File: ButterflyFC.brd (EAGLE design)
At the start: 100 x 80 mm, 7 parts

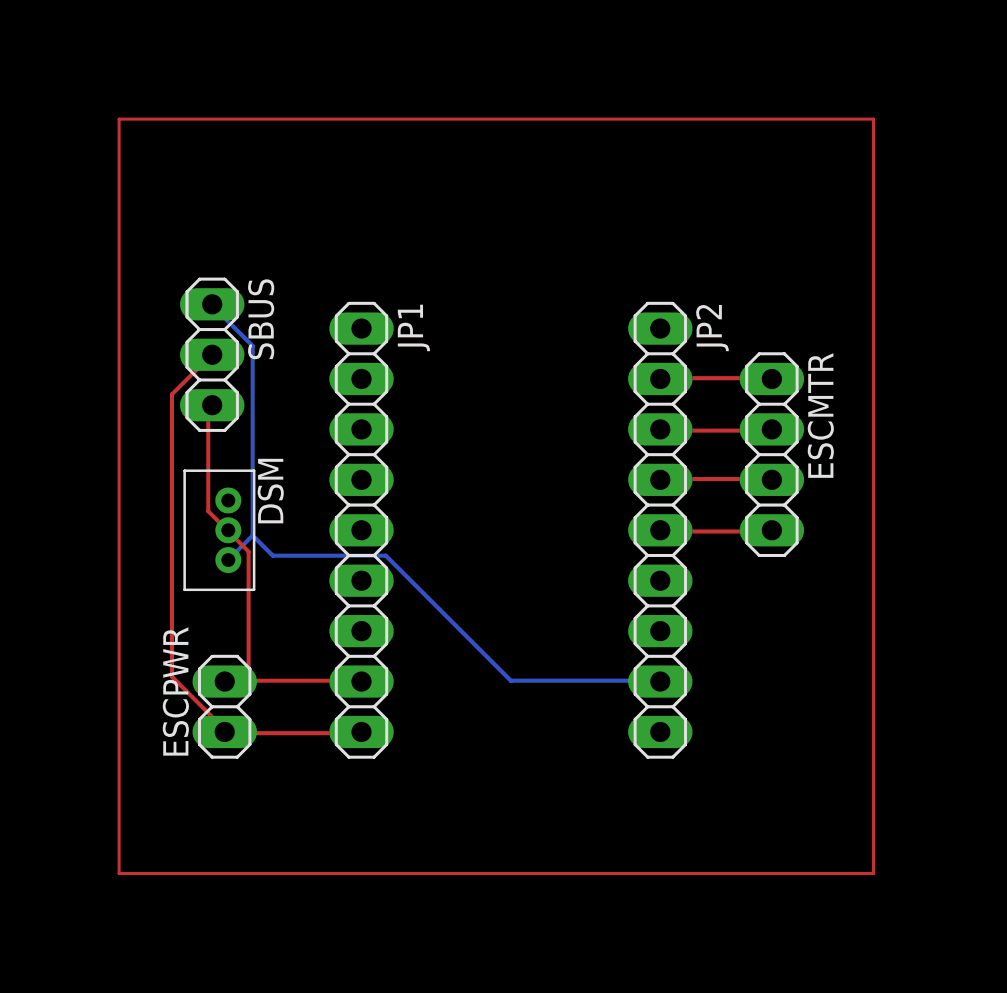
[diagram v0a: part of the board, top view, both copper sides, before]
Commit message: Restoring copper pour
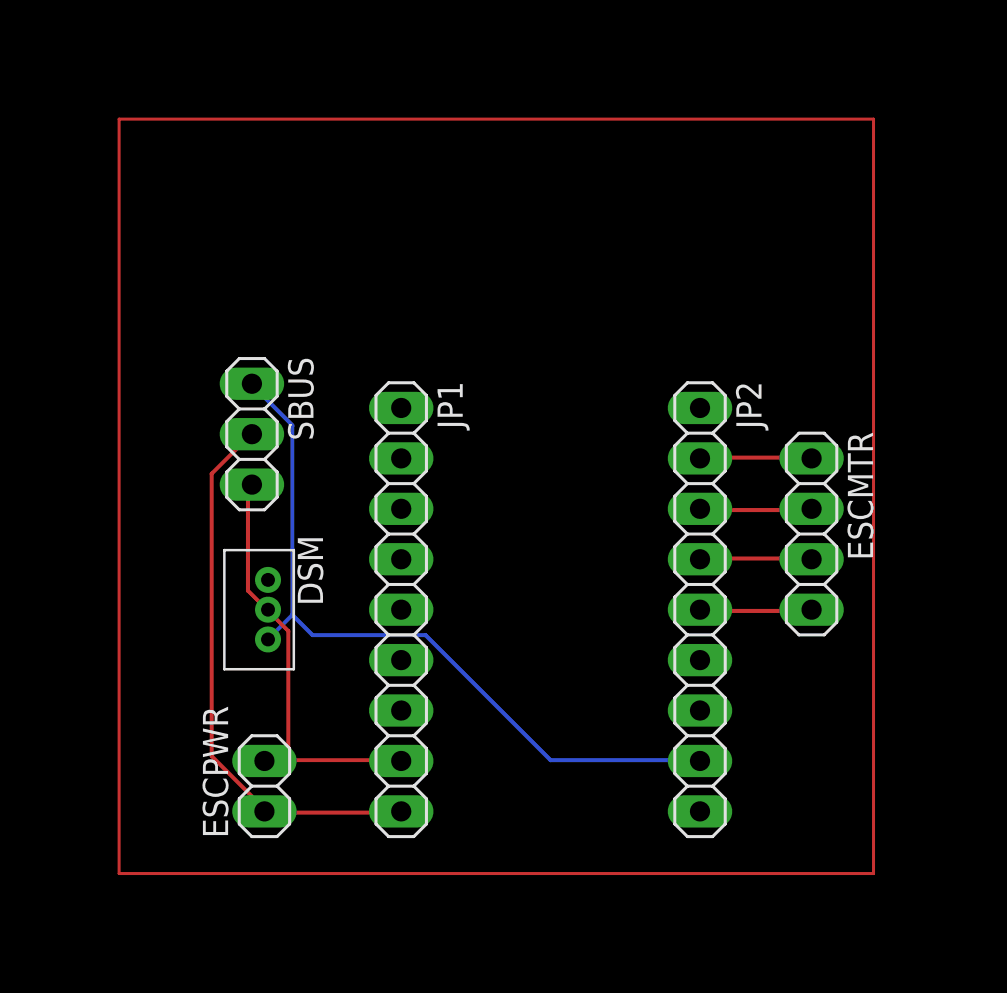
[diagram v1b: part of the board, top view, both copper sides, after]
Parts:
- moved DSM 4.47 mm to (21.5, 23.3)
- moved ESCMTR 4.47 mm to (48.9, 27.1)
- moved JP1 4.47 mm to (28.2, 23.3)
- moved JP2 4.47 mm to (43.3, 23.3)
- moved SBUS 4.47 mm to (20.7, 32.1)
- moved ESCPWR 4.47 mm to (21.3, 14.4)
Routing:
- added copper zone on layer 1, net GND

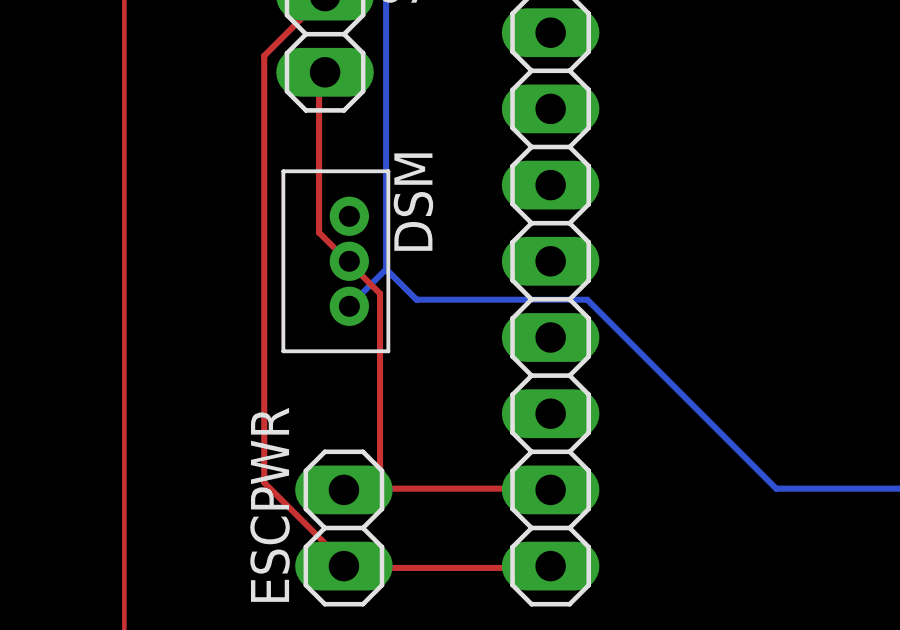
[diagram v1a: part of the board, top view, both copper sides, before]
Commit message: Fixed broken 3.3V connection
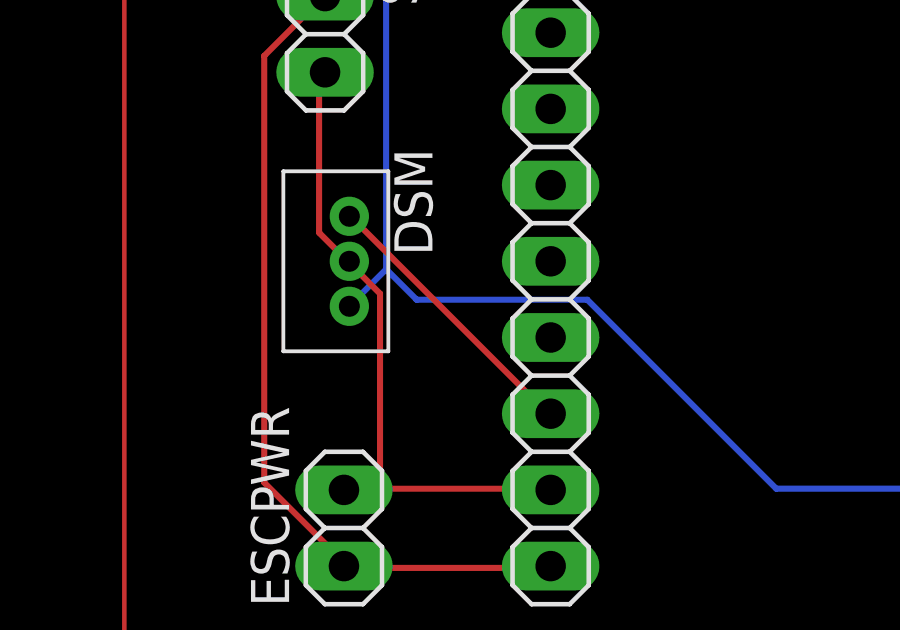
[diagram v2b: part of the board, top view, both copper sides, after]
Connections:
- removed net N$1: DSM.1
- net 3V3: now also DSM.1
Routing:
- net 3V3: track 0.00 -> 9.50 mm
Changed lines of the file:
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@@
 <wire x1="48.736" y1="25.8704" x2="48.88" y2="25.83" width="0.2032" layer="1"/>
-</signal>
-<signal name="3V3">
-<contactref element="JP1" pad="7"/>
-</signal>
-<signal name="N$1">
-<contactref element="DSM" pad="1"/>
 </signal>
 <signal name="N$2">
@@
 <wire x1="14" y1="10" x2="14" y2="48" width="0.1524" layer="1"/>
 </signal>
+<signal name="3V3">
+<contactref element="JP1" pad="7"/>
+<contactref element="DSM" pad="1"/>
+<wire x1="21.7424" y1="24.5872" x2="21.5392" y2="24.5872" width="0.2032" layer="1"/>
+<wire x1="28.0416" y1="18.288" x2="21.7424" y2="24.5872" width="0.2032" layer="1"/>
+<wire x1="21.5392" y1="24.5872" x2="21.5" y2="24.79" width="0.2032" layer="1"/>
+<wire x1="28.0416" y1="18.288" x2="28.21" y2="18.21" width="0.2032" layer="1"/>
+</signal>
 </signals>

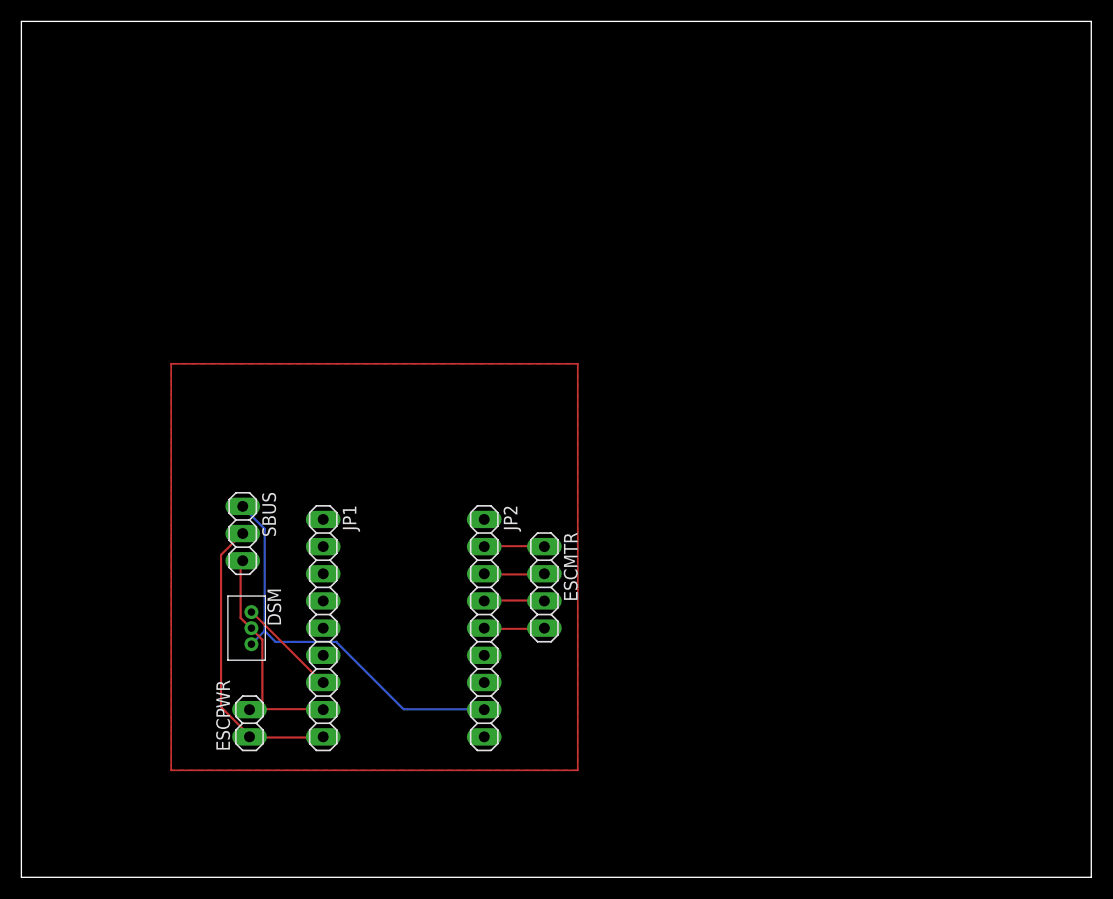
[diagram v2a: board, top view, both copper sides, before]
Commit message: Added stencil, bigger holes
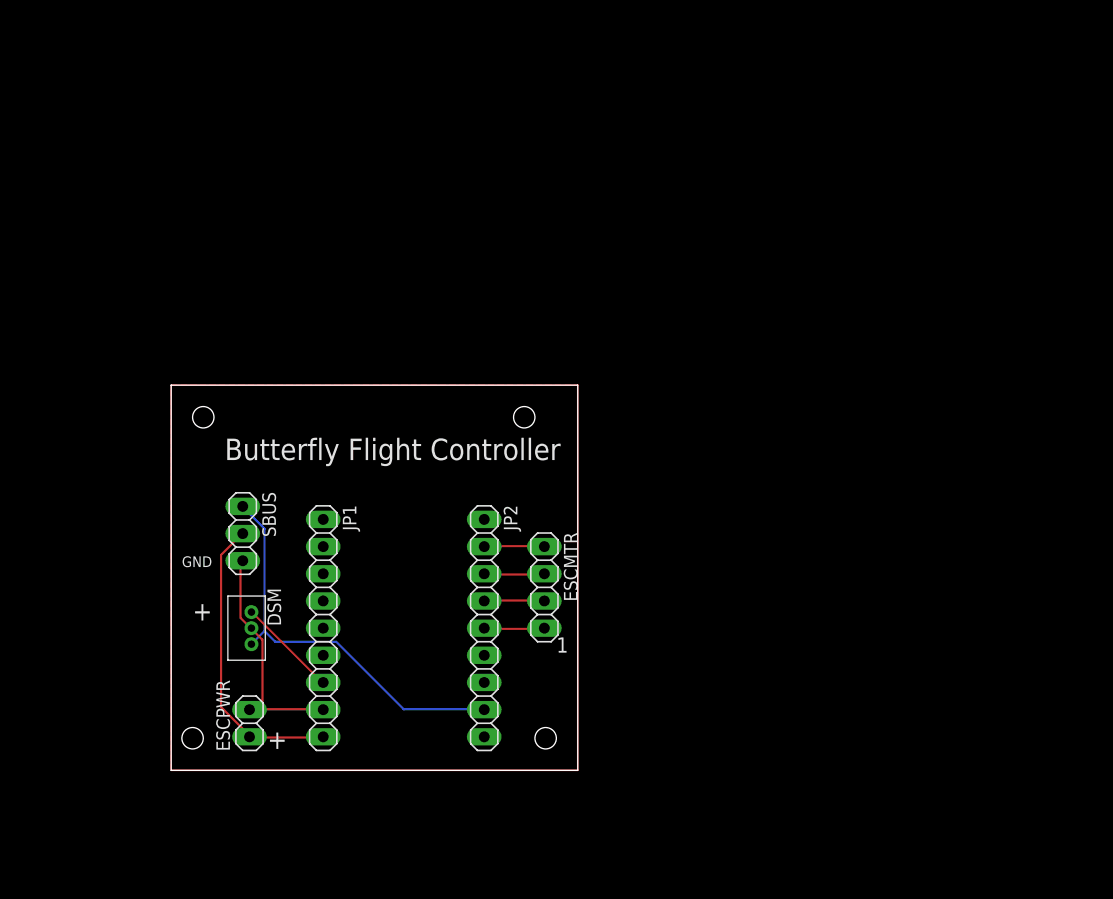
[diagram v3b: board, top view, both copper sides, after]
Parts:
- moved FRAME1 94.4 mm to (13.0, -0.76)
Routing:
- net N$5: track 152.0 -> 0.00 mm
- net GND: track 23.0 -> 171.0 mm
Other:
- board size 100 x 80 mm -> 38 x 36 mm
- board text added: "+"
- board text added: "1"
- board text added: "Butterfly Flight Controller"
- board text added: "GND"
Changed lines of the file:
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@@
 <layer number="43" name="vRestrict" color="2" fill="10" visible="yes" active="yes"/>
 <layer number="44" name="Drills" color="7" fill="1" visible="no" active="yes"/>
-<layer number="45" name="Holes" color="7" fill="1" visible="no" active="yes"/>
+<layer number="45" name="Holes" color="7" fill="1" visible="yes" active="yes"/>
 <layer number="46" name="Milling" color="3" fill="1" visible="no" active="yes"/>
 <layer number="47" name="Measures" color="7" fill="1" visible="no" active="yes"/>
@@
 <board>
 <plain>
-<wire x1="0" y1="0" x2="100" y2="0" width="0" layer="20"/>
-<wire x1="100" y1="0" x2="100" y2="80" width="0" layer="20"/>
-<wire x1="100" y1="80" x2="0" y2="80" width="0" layer="20"/>
-<wire x1="0" y1="80" x2="0" y2="0" width="0" layer="20"/>
+<wire x1="14" y1="10" x2="52" y2="10" width="0" layer="20"/>
+<wire x1="52" y1="10" x2="52" y2="46" width="0" layer="20"/>
+<wire x1="52" y1="46" x2="14" y2="46" width="0" layer="20"/>
+<wire x1="14" y1="46" x2="14" y2="10" width="0" layer="20"/>
+<hole x="17" y="43" drill="2"/>
+<hole x="47" y="43" drill="2"/>
+<hole x="49" y="13" drill="2"/>
+<hole x="16" y="13" drill="2"/>
+<text x="19" y="39" size="2" layer="21">Butterfly Flight Controller</text>
+<text x="23" y="12" size="1.778" layer="21">+</text>
+<text x="16" y="24" size="1.778" layer="21">+</text>
+<text x="15" y="29" size="1" layer="21">GND</text>
+<text x="50" y="21" size="1.4224" layer="21" font="fixed">1</text>
 </plain>
 <attributes>
@@
 <element name="DSM" library="jst" package="B3B-ZR" value="B3B-ZR" x="21.5" y="23.29" rot="R270"/>
 <element name="ESCMTR" library="pinhead" library_urn="urn:adsk.eagle:library:325" package="1X04" package3d_urn="urn:adsk.eagle:package:22407/2" value="" x="48.88" y="27.1" rot="R270"/>
-<element name="FRAME1" library="SparkFun-Aesthetics" library_urn="urn:adsk.eagle:library:507" package="CREATIVE_COMMONS" package3d_urn="urn:adsk.eagle:package:37121/1" value="FRAME-LETTER" x="-80.01" y="15.24"/>
+<element name="FRAME1" library="SparkFun-Aesthetics" library_urn="urn:adsk.eagle:library:507" package="CREATIVE_COMMONS" package3d_urn="urn:adsk.eagle:package:37121/1" value="FRAME-LETTER" x="12.99" y="-0.76"/>
 <element name="JP1" library="pinhead" library_urn="urn:adsk.eagle:library:325" package="1X09" package3d_urn="urn:adsk.eagle:package:22483/2" value="" x="28.21" y="23.29" rot="R270"/>
 <element name="JP2" library="pinhead" library_urn="urn:adsk.eagle:library:325" package="1X09" package3d_urn="urn:adsk.eagle:package:22483/2" value="" x="43.26" y="23.29" rot="R270"/>
@@
 <wire x1="22.5232" y1="15.7104" x2="21.32" y2="15.67" width="0.2032" layer="1"/>
 <polygon width="0.3048" layer="1" isolate="0.3048">
-<vertex x="14" y="48"/>
-<vertex x="52" y="48"/>
+<vertex x="14" y="46"/>
+<vertex x="52" y="46"/>
 <vertex x="52" y="10"/>
 <vertex x="14" y="10"/>
 </polygon>
+<wire x1="14" y1="46" x2="52" y2="46" width="0.1524" layer="1"/>
+<wire x1="52" y1="46" x2="52" y2="10" width="0.1524" layer="1"/>
+<wire x1="52" y1="10" x2="14" y2="10" width="0.1524" layer="1"/>
+<wire x1="14" y1="10" x2="14" y2="46" width="0.1524" layer="1"/>
+<wire x1="21.32" y1="15.67" x2="14" y2="10" width="0" layer="19" extent="1-1"/>
 </signal>
 <signal name="VCC">
@@
 <wire x1="48.736" y1="28.3088" x2="48.88" y2="28.37" width="0.2032" layer="1"/>
 </signal>
-<signal name="N$5">
-<wire x1="14" y1="48" x2="52" y2="48" width="0.1524" layer="1"/>
-<wire x1="52" y1="48" x2="52" y2="10" width="0.1524" layer="1"/>
-<wire x1="52" y1="10" x2="14" y2="10" width="0.1524" layer="1"/>
-<wire x1="14" y1="10" x2="14" y2="48" width="0.1524" layer="1"/>
-</signal>
 <signal name="3V3">
